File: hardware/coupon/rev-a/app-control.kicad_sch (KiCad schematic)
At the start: 1 part, among them SW2 JS202011JCQN

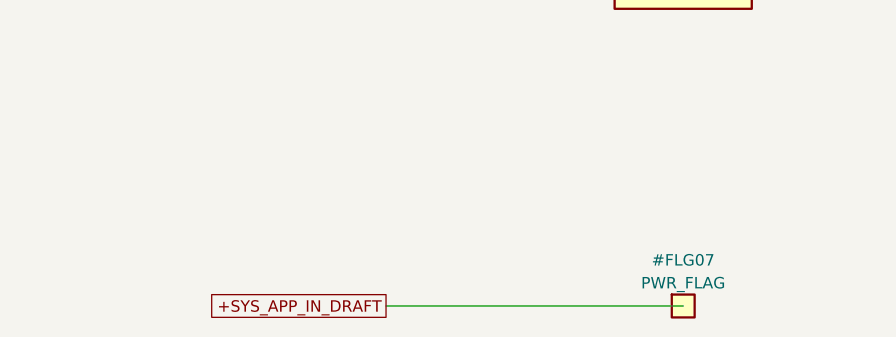
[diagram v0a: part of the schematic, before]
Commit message: Connect provisional BQ24074 charger core to battery NTC
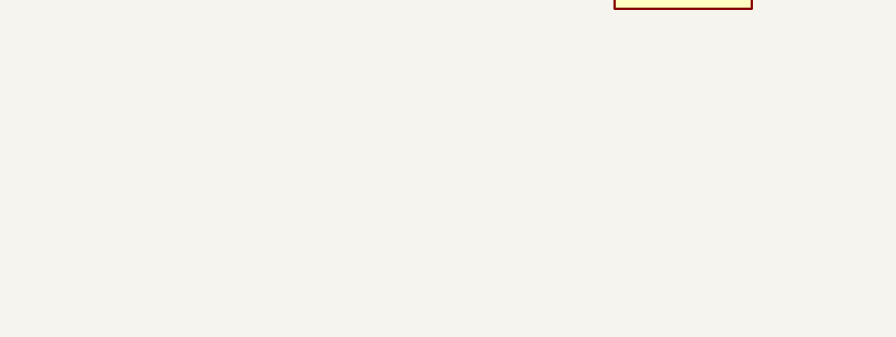
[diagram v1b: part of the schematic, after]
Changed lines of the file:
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@@
 (generator_version "1.0")
 (paper "A4")
-(title_block (title "Coupon Rev A - provisional application control") (rev "A-draft") (comment 1 "SPDX-License-Identifier: CERN-OHL-S-2.0") (comment 2 "SYS PWR_FLAG is an unresolved charger OUT boundary; no fabrication"))
+(title_block (title "Coupon Rev A - provisional application control") (rev "A-draft") (comment 1 "SPDX-License-Identifier: CERN-OHL-S-2.0") (comment 2 "Charger OUT source staged; no fabrication"))
 (text "Pole 1 drives TPS631000 EN with a separate 100k OFF pull-down on the converter page." (at 20.320 20.320 0) (effects (font (size 1.27 1.27)) (justify left)))
 (text "Pole 2 is reserved for the gauge; leave it open until I2C isolation and contact order are reviewed." (at 20.320 27.940 0) (effects (font (size 1.27 1.27)) (justify left)))
@@
 (no_connect (at 110.490 93.980))
 (no_connect (at 130.810 96.520))
-(symbol (lib_id "rgb-badge-coupon:PWR_FLAG") (at 120.650 132.080 0) (unit 1)
-(exclude_from_sim no) (in_bom no) (on_board no) (dnp no)
-(property "Reference" "#FLG07" (at 120.650 127.000 0) (effects (font (size 1.27 1.27))))
-(property "Value" "PWR_FLAG" (at 120.650 129.540 0) (effects (font (size 1.27 1.27))))
-(property "Footprint" "" (at 120.650 132.080 0) (effects (font (size 1.27 1.27)) (hide yes)))
-(property "Datasheet" "" (at 120.650 132.080 0) (effects (font (size 1.27 1.27)) (hide yes)))
-(property "Manufacturer" "" (at 120.650 132.080 0) (effects (font (size 1.27 1.27)) (hide yes)))
-(property "MPN" "" (at 120.650 132.080 0) (effects (font (size 1.27 1.27)) (hide yes)))
-(pin "1")
-(instances (project "rgb-badge-coupon" (path "/207fb68e-2ddb-46bb-8712-eba2f8c5eef6/6dbe5759-c45c-55eb-b787-20e70dd36eac" (reference "#FLG07") (unit 1)))))
-(wire (pts (xy 120.650 132.080) (xy 87.630 132.080)) (stroke (width 0) (type default)))
-(global_label "+SYS_APP_IN_DRAFT" (shape passive) (at 87.630 132.080 180) (effects (font (size 1.27 1.27)) (justify right)) (property "Intersheetrefs" "${INTERSHEET_REFS}" (at 87.630 132.080 0) (effects (font (size 1.27 1.27)) (hide yes))))
 (embedded_fonts no)
 )

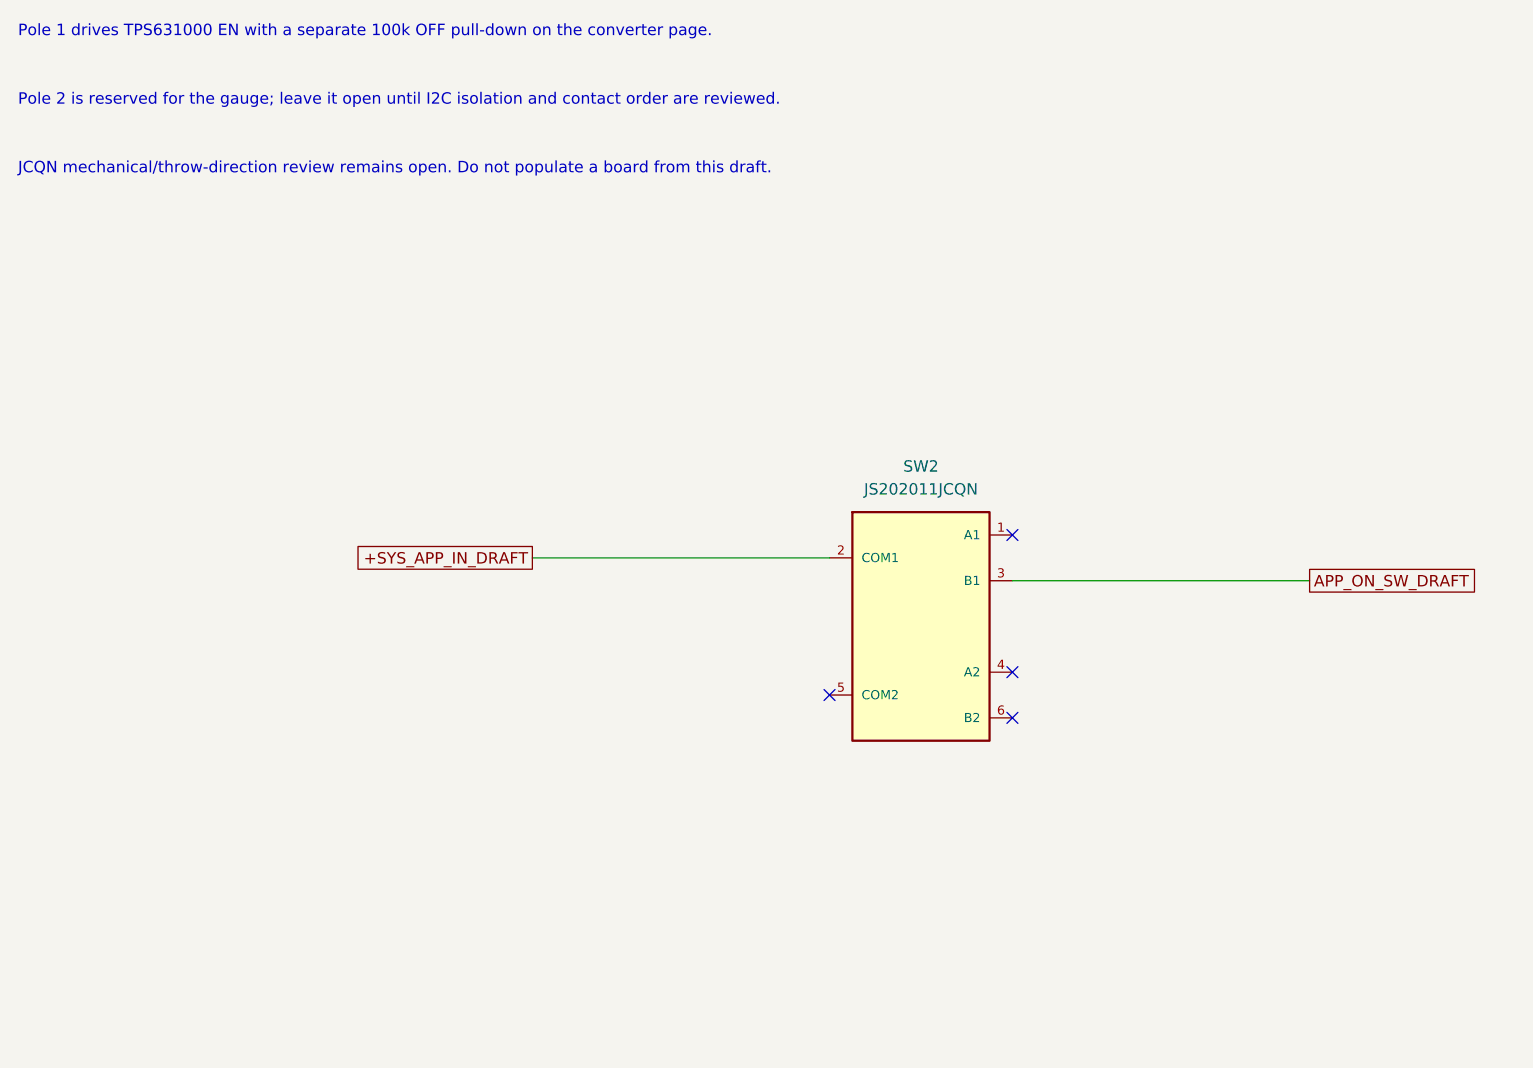
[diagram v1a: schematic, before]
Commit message: Connect switched gauge through isolated I2C buffer
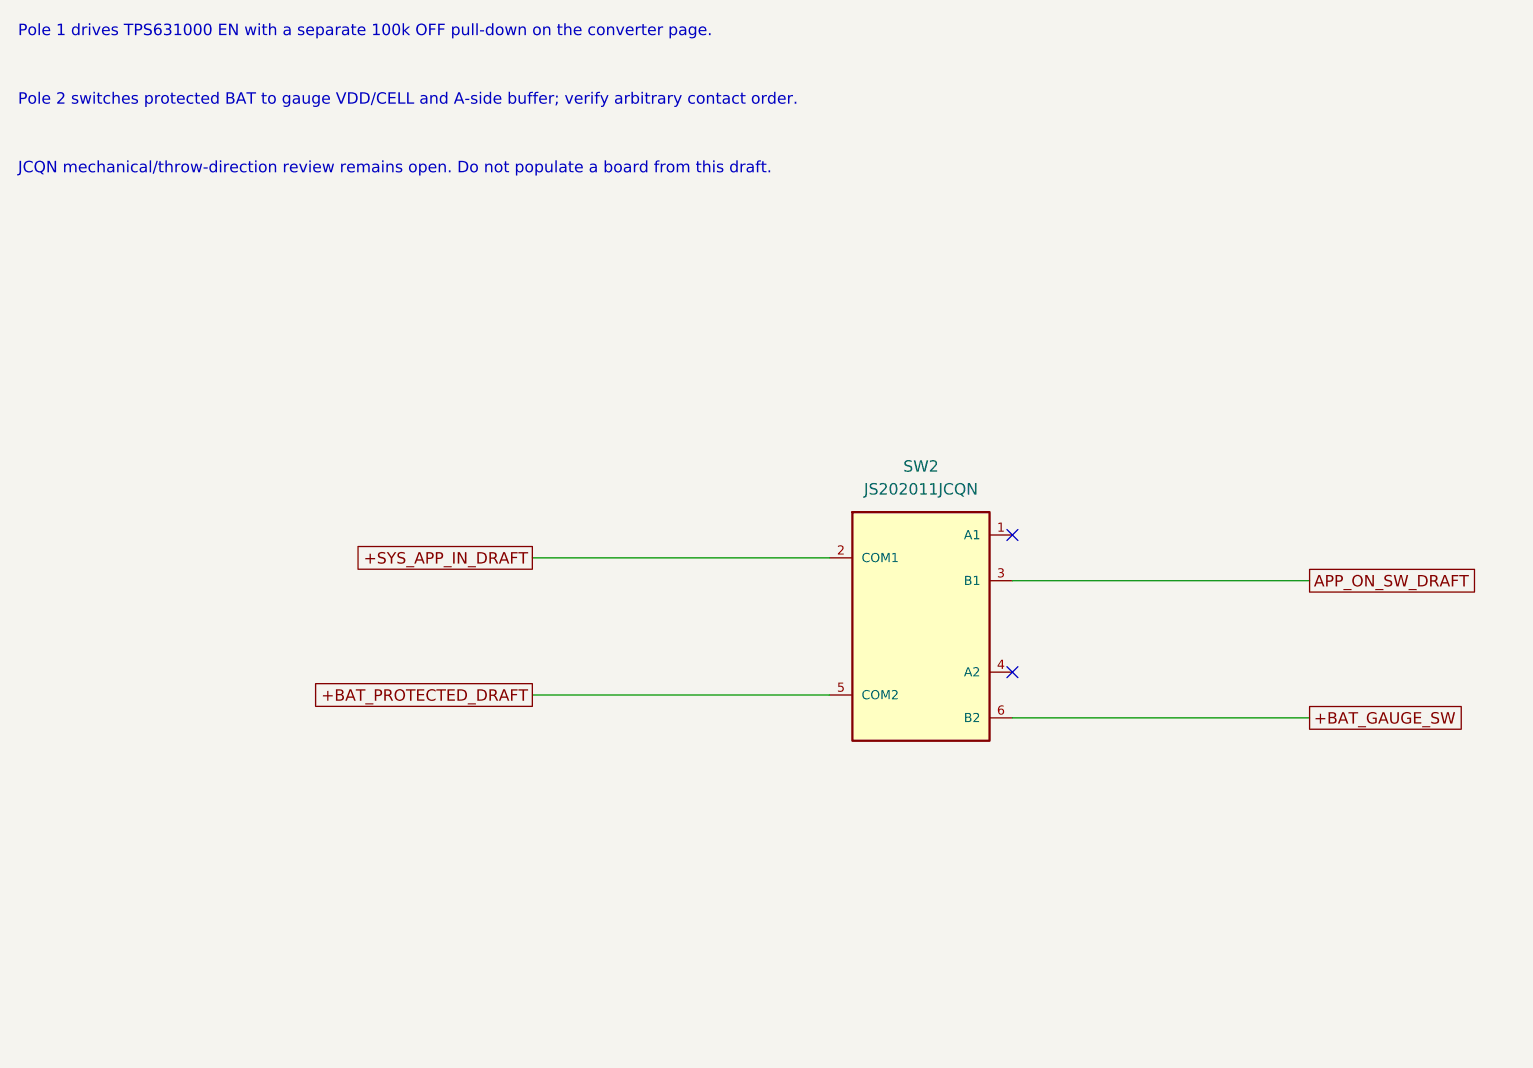
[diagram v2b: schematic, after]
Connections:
- net +BAT_PROTECTED_DRAFT: now reaches SW2.5 (COM2)
- net +BAT_GAUGE_SW: now reaches SW2.6 (B2)
- no-connect marks 4 -> 2
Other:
- note added: "Pole 2 switches protected BAT to gauge VDD/CELL and A-side buffer; verify arbitrary contact order."
- note removed: "Pole 2 is reserved for the gauge; leave it open until I2C isolation and contact order are reviewed."
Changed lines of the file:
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@@
 (title_block (title "Coupon Rev A - provisional application control") (rev "A-draft") (comment 1 "SPDX-License-Identifier: CERN-OHL-S-2.0") (comment 2 "Charger OUT source staged; no fabrication"))
 (text "Pole 1 drives TPS631000 EN with a separate 100k OFF pull-down on the converter page." (at 20.320 20.320 0) (effects (font (size 1.27 1.27)) (justify left)))
-(text "Pole 2 is reserved for the gauge; leave it open until I2C isolation and contact order are reviewed." (at 20.320 27.940 0) (effects (font (size 1.27 1.27)) (justify left)))
+(text "Pole 2 switches protected BAT to gauge VDD/CELL and A-side buffer; verify arbitrary contact order." (at 20.320 27.940 0) (effects (font (size 1.27 1.27)) (justify left)))
 (text "JCQN mechanical/throw-direction review remains open. Do not populate a board from this draft." (at 20.320 35.560 0) (effects (font (size 1.27 1.27)) (justify left)))
 (symbol (lib_id "rgb-badge-coupon:JS202011JCQN") (at 120.650 86.360 0) (unit 1)
@@
 (wire (pts (xy 130.810 81.280) (xy 163.830 81.280)) (stroke (width 0) (type default)))
 (global_label "APP_ON_SW_DRAFT" (shape passive) (at 163.830 81.280 0) (effects (font (size 1.27 1.27)) (justify left)) (property "Intersheetrefs" "${INTERSHEET_REFS}" (at 163.830 81.280 0) (effects (font (size 1.27 1.27)) (hide yes))))
+(wire (pts (xy 110.490 93.980) (xy 77.470 93.980)) (stroke (width 0) (type default)))
+(global_label "+BAT_PROTECTED_DRAFT" (shape passive) (at 77.470 93.980 180) (effects (font (size 1.27 1.27)) (justify right)) (property "Intersheetrefs" "${INTERSHEET_REFS}" (at 77.470 93.980 0) (effects (font (size 1.27 1.27)) (hide yes))))
+(wire (pts (xy 130.810 96.520) (xy 163.830 96.520)) (stroke (width 0) (type default)))
+(global_label "+BAT_GAUGE_SW" (shape passive) (at 163.830 96.520 0) (effects (font (size 1.27 1.27)) (justify left)) (property "Intersheetrefs" "${INTERSHEET_REFS}" (at 163.830 96.520 0) (effects (font (size 1.27 1.27)) (hide yes))))
 (no_connect (at 130.810 76.200))
 (no_connect (at 130.810 91.440))
-(no_connect (at 110.490 93.980))
-(no_connect (at 130.810 96.520))
 (embedded_fonts no)
 )

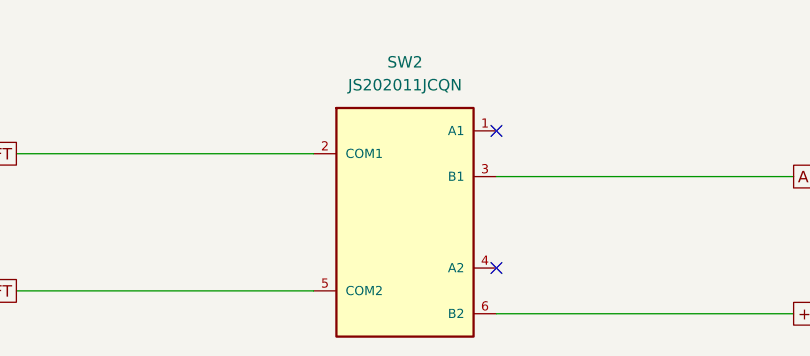
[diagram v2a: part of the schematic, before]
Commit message: Join gauge switch supply at 58 opens and correct printed switch terminals
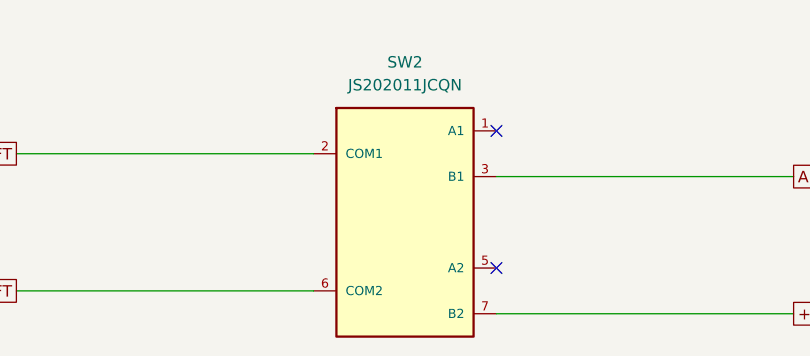
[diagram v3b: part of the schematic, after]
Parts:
- SW2: footprint rgb-badge-coupon:SW_CK_JS202011JCQN -> rgb-badge-coupon:SW_CK_JS202011JCQN_ManufacturerPins
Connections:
- net +BAT_GAUGE_SW: now also SW2.7 (B2); no longer SW2.6 (B2)
- net +BAT_PROTECTED_DRAFT: now also SW2.6 (COM2); no longer SW2.5 (COM2)
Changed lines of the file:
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@@
 (property "Reference" "SW2" (at 120.650 68.580 0) (effects (font (size 1.27 1.27))))
 (property "Value" "JS202011JCQN" (at 120.650 71.120 0) (effects (font (size 1.27 1.27))))
-(property "Footprint" "rgb-badge-coupon:SW_CK_JS202011JCQN" (at 120.650 86.360 0) (effects (font (size 1.27 1.27)) (hide yes)))
+(property "Footprint" "rgb-badge-coupon:SW_CK_JS202011JCQN_ManufacturerPins" (at 120.650 86.360 0) (effects (font (size 1.27 1.27)) (hide yes)))
 (property "Datasheet" "https://www.ckswitches.com/media/1422/js.pdf" (at 120.650 86.360 0) (effects (font (size 1.27 1.27)) (hide yes)))
 (property "Manufacturer" "C&K / Littelfuse" (at 120.650 86.360 0) (effects (font (size 1.27 1.27)) (hide yes)))
@@
 (pin "2")
 (pin "3")
-(pin "4")
 (pin "5")
 (pin "6")
+(pin "7")
 (instances (project "rgb-badge-coupon" (path "/207fb68e-2ddb-46bb-8712-eba2f8c5eef6/6dbe5759-c45c-55eb-b787-20e70dd36eac" (reference "SW2") (unit 1)))))
 (wire (pts (xy 110.490 78.740) (xy 77.470 78.740)) (stroke (width 0) (type default)))
